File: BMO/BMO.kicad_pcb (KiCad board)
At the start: 4 copper layers, 82 x 89.5 mm, 133 parts, among them J1 EXT, J10 USB_C_Receptacle_USB2.0_16P, J11 BAT, J12 Conn_01x06, J13 SERVO, J14 Conn_01x06, J15 ON/OFF, J2 Conn_ST_STDC14, J3 TOF1_VL53L0X, J4 TOF2_VL53L0X, J5 COULEUR_I2C, J6 NEOPIXEL, J7 LIDAR_X2, J8 OLED_I2C, J9 Conn_01x06, Q1 MMDT2907A-7-F, Q2 DMP1045U-7, Q3 DMN313DLT-7, SW1 USER, SW2 SW_Push, SW3 nQON, U1 STM32G474RBTx, U2 MPU-6050, U3 SN74AHCT1G125DBVR, U4 USBLC6-2SC6, U5 AP2112K-3.3, U6 BQ27220YZFR, U7 BQ25896RTW, U8 DRV8833PWPR, Y1 16MHz

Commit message: Finalize PCB design and generate BOM and CPL files
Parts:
- added G***: LOGO, LOGO, F.Cu at (158.2, 118.3)
- renumbered TP7 to 3V3, TP10 to 3V3A, TP5 to 5V, C9 to C10, C10 to C11, C11 to C12, C12 to C13, C13 to C14, C14 to C15, C15 to C16, C16 to C17, C17 to C18, C18 to C19, C19 to C20, C20 to C21, C21 to C22, C22 to C23, C23 to C24, C24 to C25, C25 to C26, C26 to C27, C27 to C28, C28 to C29, C29 to C30, C30 to C31, C31 to C32, C32 to C33, C33 to C34, C34 to C35, C35 to C36, C36 to C37, C37 to C38, C38 to C39, C45 to C4, C39 to C40, C40 to C41, C41 to C42, C42 to C43, C43 to C44, C44 to C45, C4 to C5, C5 to C6, C6 to C7, C7 to C8, C8 to C9, J15 to J12, J12 to J13, J13 to J14, J14 to J15, R14 to R13, R16 to R14, R17 to R15, R18 to R16, R19 to R17, R20 to R18, R21 to R19, R22 to R20, R23 to R21, R24 to R22, R25 to R23, R26 to R24, R27 to R25, R28 to R26, R29 to R27, R30 to R28, R31 to R29, R32 to R30, R33 to R31, TP9 to SYS, TP11 to TP4, TP4 to TP5, TP8 to VBAT, TP6 to VBUS
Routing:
- net /STM32G474RBT3/TOF1_INT: track 45.1 -> 42.7 mm, vias 2 -> 0
- net GND: vias 331 -> 393
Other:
- board text added: "Component"
- board text added: "Directly Below"
- board text added: "KEEPOUT"
- board text added: "No Copper"
- board text added: "U2"
- board text added: "Watchdog: I'm watching you ! ಠ_ಠ"
- board text removed: "C34"
- board text removed: "R24"

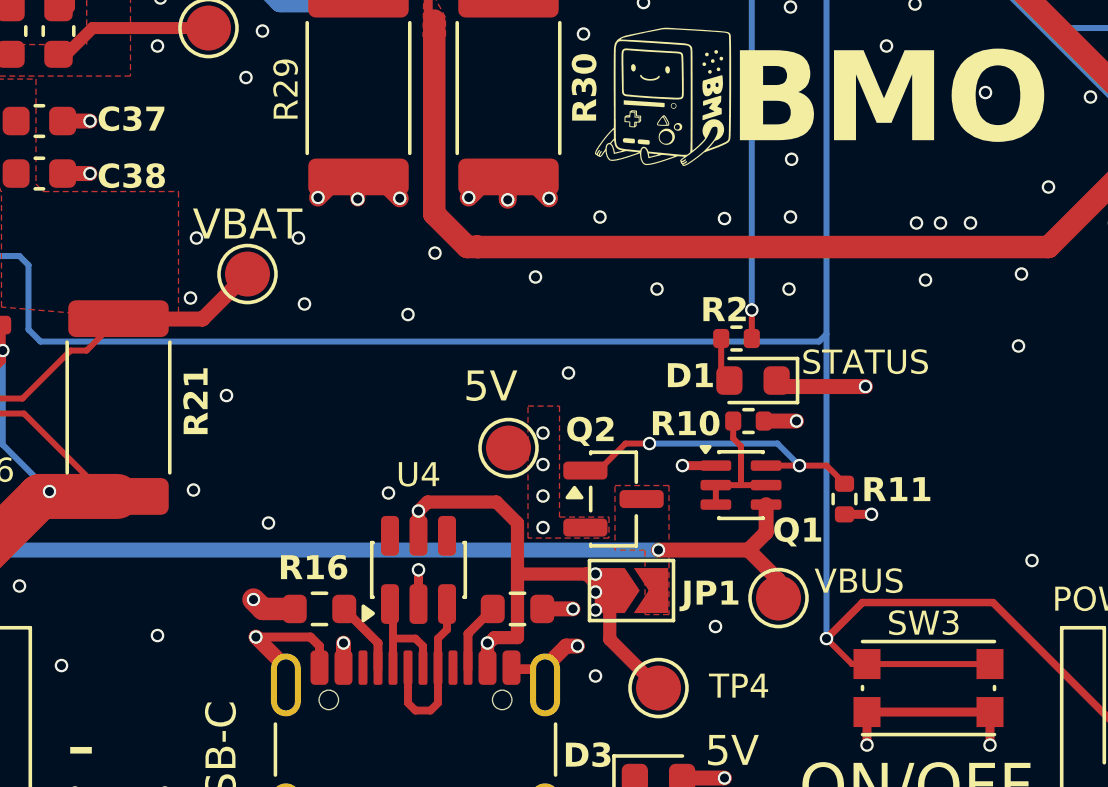
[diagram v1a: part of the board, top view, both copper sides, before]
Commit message: Update USB-C connector to in-stock part, align CPL coordinates and finalize BOM
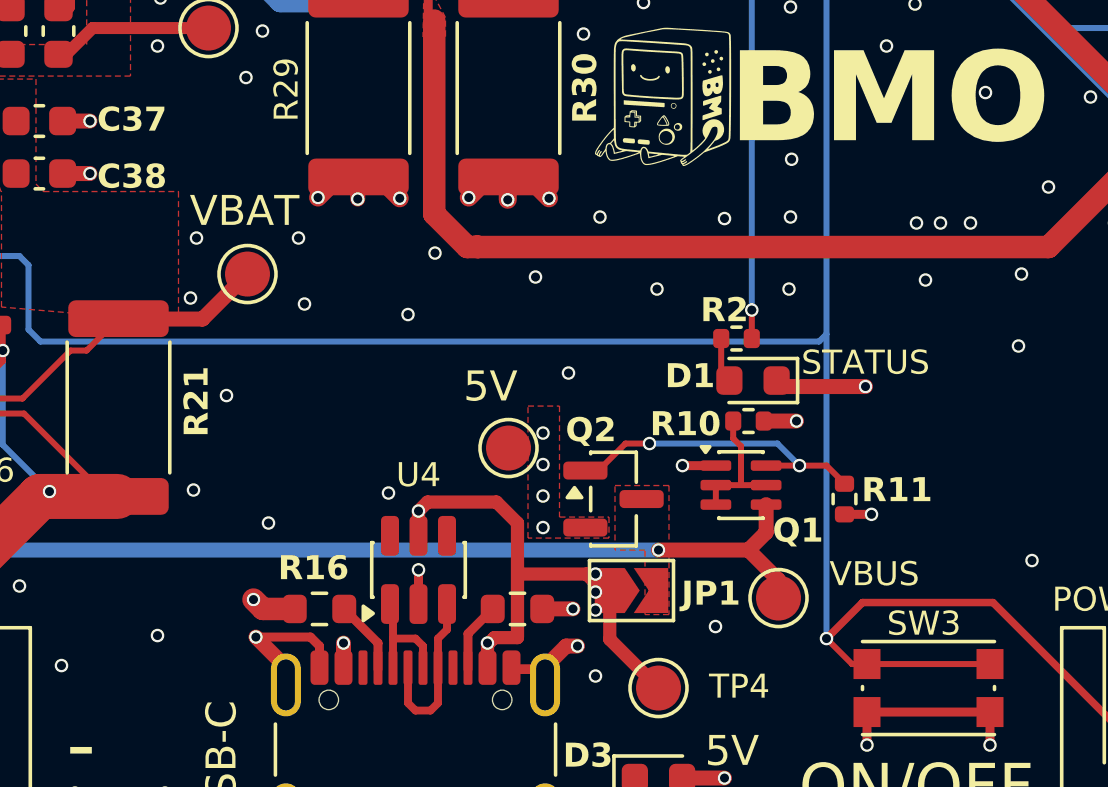
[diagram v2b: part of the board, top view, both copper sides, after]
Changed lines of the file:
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@@
 		(tags "test point SMD pad")
 		(property "Reference" "VBAT"
-			(at 0 -1.648 0)
+			(at -0.1 -2.1 0)
 			(layer "F.SilkS")
 			(effects
@@
 			)
 		)
-		(property "JLCPCB Part #" "C3020560"
+		(property "JLCPCB Part #" "C5184243"
 			(at 0 0 0)
 			(layer "F.Fab")
@@
 		(tags "test point SMD pad")
 		(property "Reference" "VBUS"
-			(at 2.7 -0.55 0)
+			(at 3.2 -0.8 0)
 			(layer "F.SilkS")
 			(effects
@@
 		(layer "F.Cu")
 		(hatch none 0.1)
-		(priority 30052)
+		(priority 30090)
 		(attr
 			(teardrop
@@
 		(polygon
 			(pts
-				(xy 165.85 137.3) (xy 165.85 137.1) (xy 165.4 136.75) (xy 164.949 137.2) (xy 165.4 137.65)
+				(xy 164.45 137.1) (xy 164.45 137.3) (xy 164.5 137.65) (xy 164.951 137.2) (xy 164.5 136.75)
 			)
 		)
@@
 		(layer "F.Cu")
 		(hatch none 0.1)
-		(priority 30090)
+		(priority 30052)
 		(attr
 			(teardrop
@@
 		(polygon
 			(pts
-				(xy 164.45 137.1) (xy 164.45 137.3) (xy 164.5 137.65) (xy 164.951 137.2) (xy 164.5 136.75)
+				(xy 165.85 137.3) (xy 165.85 137.1) (xy 165.4 136.75) (xy 164.949 137.2) (xy 165.4 137.65)
 			)
 		)
@@
 		(layer "F.Cu")
 		(hatch none 0.1)
-		(priority 30183)
+		(priority 30110)
 		(attr
 			(teardrop
@@
 		(polygon
 			(pts
-				(xy 134.018001 126.23119) (xy 134.267999 126.230809) (xy 134.336076 126.199343) (xy 134.142494 125.899)
-				(xy 133.948924 126.199343)
+				(xy 134.267794 125.310063) (xy 134.017796 125.309938) (xy 133.873157 125.676424) (xy 134.1425 125.901)
+				(xy 134.411843 125.676424)
 			)
 		)
@@
 		(layer "F.Cu")
 		(hatch none 0.1)
-		(priority 30110)
+		(priority 30183)
 		(attr
 			(teardrop
@@
 		(polygon
 			(pts
-				(xy 134.267794 125.310063) (xy 134.017796 125.309938) (xy 133.873157 125.676424) (xy 134.1425 125.901)
-				(xy 134.411843 125.676424)
+				(xy 134.018001 126.23119) (xy 134.267999 126.230809) (xy 134.336076 126.199343) (xy 134.142494 125.899)
+				(xy 133.948924 126.199343)
 			)
 		)
